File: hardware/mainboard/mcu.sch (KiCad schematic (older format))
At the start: 20 parts, among them J2 Tag-Connect SWD, J3 USB_MICRO_RIGHT, SW1 RESET, U7 ATSAMD21G18A-AUT, U8 MCP4728

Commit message: Create hardware revision mainboard v3
This addresses an issue with the ramp oscillators using the wrong type of transistor.
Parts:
- J2, TP3, TP4, TP5, TP6, TP7: dnp (none) -> 1; finalized (none) -> yes
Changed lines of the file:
@@
 Sheet 6 7
 Title "Castor & Pollux"
-Date "2020-09-26"
-Rev "v2"
+Date "2021-01-27"
+Rev "v3"
 Comp "Winterbloom"
 Comment1 "CERN-OHL-P v2"
@@
 F 2 "Connector:Tag-Connect_TC2030-IDC-NL_2x03_P1.27mm_Vertical" H 5400 7100 50  0001 C CNN
 F 3 "~" H 5400 7100 50  0001 C CNN
-F 4 "" H 5400 7100 50  0001 C CNN "finalized"
+F 4 "yes" H 5400 7100 50  0001 C CNN "finalized"
+F 5 "1" H 5400 7100 50  0001 C CNN "dnp"
 	1    5400 7100
 	1    0    0    -1
@@
 F 2 "TestPoint:TestPoint_Pad_D1.0mm" H 8050 1000 50  0001 C CNN
 F 3 "~" H 8050 1000 50  0001 C CNN
+F 4 "1" H 7850 1000 50  0001 C CNN "dnp"
+F 5 "yes" H 7850 1000 50  0001 C CNN "finalized"
 	1    7850 1000
 	0    1    1    0
@@
 F 2 "TestPoint:TestPoint_Pad_D1.0mm" H 8050 1200 50  0001 C CNN
 F 3 "~" H 8050 1200 50  0001 C CNN
+F 4 "1" H 7850 1200 50  0001 C CNN "dnp"
+F 5 "yes" H 7850 1200 50  0001 C CNN "finalized"
 	1    7850 1200
 	0    1    1    0
@@
 F 2 "TestPoint:TestPoint_Pad_D1.0mm" H 5450 7450 50  0001 C CNN
 F 3 "~" H 5450 7450 50  0001 C CNN
+F 4 "1" H 5250 7450 50  0001 C CNN "dnp"
+F 5 "yes" H 5250 7450 50  0001 C CNN "finalized"
 	1    5250 7450
 	0    1    1    0
@@
 F 2 "TestPoint:TestPoint_Pad_D1.0mm" H 5450 7650 50  0001 C CNN
 F 3 "~" H 5450 7650 50  0001 C CNN
+F 4 "1" H 5250 7650 50  0001 C CNN "dnp"
+F 5 "yes" H 5250 7650 50  0001 C CNN "finalized"
 	1    5250 7650
 	0    1    1    0
@@
 F 2 "TestPoint:TestPoint_Pad_D1.0mm" H 5450 7850 50  0001 C CNN
 F 3 "~" H 5450 7850 50  0001 C CNN
+F 4 "1" H 5250 7850 50  0001 C CNN "dnp"
+F 5 "yes" H 5250 7850 50  0001 C CNN "finalized"
 	1    5250 7850
 	0    1    1    0

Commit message: hardware: finalize v3 of mainboard for production
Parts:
- C18, C19, C20, C21, C22, C49, C50: Reqs (none) -> bypass
- C23: Reqs (none) -> audio path; mpn GRM21BR61E106KA73K -> CL21A106KAYNNNG; mpn alt (none) -> GRM21BR61E106KA73K
- R24, R25: Reqs (none) -> i2c pullup
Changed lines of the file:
@@
 Sheet 6 7
 Title "Castor & Pollux"
-Date "2021-02-01"
+Date "2021-02-05"
 Rev "v3"
 Comp "Winterbloom"
@@
 F 6 "10%, 25v" H 3050 1650 50  0001 C CNN "mpn specs"
 F 7 "GCM188R71E105KA64D" H 3050 1650 50  0001 C CNN "mpn alt"
+F 8 "bypass" H 3050 1650 50  0001 C CNN "Reqs"
 	1    3050 1650
 	1    0    0    -1
@@
 F 6 "10%, 25v" H 3150 7000 50  0001 C CNN "mpn specs"
 F 7 "GCM188R91E104KA37D" H 3150 7000 50  0001 C CNN "mpn alt"
+F 8 "bypass" H 3150 7000 50  0001 C CNN "Reqs"
 	1    3150 7000
 	1    0    0    -1
@@
 F 6 "10%, 25v" H 3650 7000 50  0001 C CNN "mpn specs"
 F 7 "GCM188R91E104KA37D" H 3650 7000 50  0001 C CNN "mpn alt"
+F 8 "bypass" H 3650 7000 50  0001 C CNN "Reqs"
 	1    3650 7000
 	1    0    0    -1
@@
 F 6 "10%, 25v" H 4150 7000 50  0001 C CNN "mpn specs"
 F 7 "GCM188R91E104KA37D" H 4150 7000 50  0001 C CNN "mpn alt"
+F 8 "bypass" H 4150 7000 50  0001 C CNN "Reqs"
 	1    4150 7000
 	1    0    0    -1
@@
 F 6 "100mW" H 4800 5900 50  0001 C CNN "mpn specs"
 F 7 "ERA-3AED472V" H 4800 5900 50  0001 C CNN "mpn alt"
+F 8 "i2c pullup" H 4800 5900 50  0001 C CNN "Reqs"
 	1    4800 5900
 	1    0    0    -1
@@
 F 6 "100mW" H 5200 5900 50  0001 C CNN "mpn specs"
 F 7 "ERA-3AED472V" H 5200 5900 50  0001 C CNN "mpn alt"
+F 8 "i2c pullup" H 5200 5900 50  0001 C CNN "Reqs"
 	1    5200 5900
 	1    0    0    -1
@@
 F 6 "10%, 25v" H 7750 5900 50  0001 C CNN "mpn specs"
 F 7 "GCM188R91E104KA37D" H 7750 5900 50  0001 C CNN "mpn alt"
+F 8 "bypass" H 7750 5900 50  0001 C CNN "Reqs"
 	1    7750 5900
 	1    0    0    -1
@@
 F 3 "~" H 8300 5900 50  0001 C CNN
 F 4 "yes" H 8300 5900 50  0001 C CNN "finalized"
-F 5 "GRM21BR61E106KA73K" H 8300 5900 50  0001 C CNN "mpn"
+F 5 "CL21A106KAYNNNG" H 8300 5900 50  0001 C CNN "mpn"
 F 6 "10% 16v" H 8300 5900 50  0001 C CNN "mpn specs"
-F 7 "" H 8300 5900 50  0001 C CNN "mpn alt"
+F 7 "GRM21BR61E106KA73K" H 8300 5900 50  0001 C CNN "mpn alt"
+F 8 "audio path" H 8300 5900 50  0001 C CNN "Reqs"
 	1    8300 5900
 	1    0    0    -1
@@
 F 6 "10%, 25v" H 2700 7000 50  0001 C CNN "mpn specs"
 F 7 "GCM188R91E104KA37D" H 2700 7000 50  0001 C CNN "mpn alt"
+F 8 "bypass" H 2700 7000 50  0001 C CNN "Reqs"
 	1    2700 7000
 	1    0    0    -1
@@
 F 6 "10%, 25v" H 2250 7000 50  0001 C CNN "mpn specs"
 F 7 "GCM188R91E104KA37D" H 2250 7000 50  0001 C CNN "mpn alt"
+F 8 "bypass" H 2250 7000 50  0001 C CNN "Reqs"
 	1    2250 7000
 	1    0    0    -1

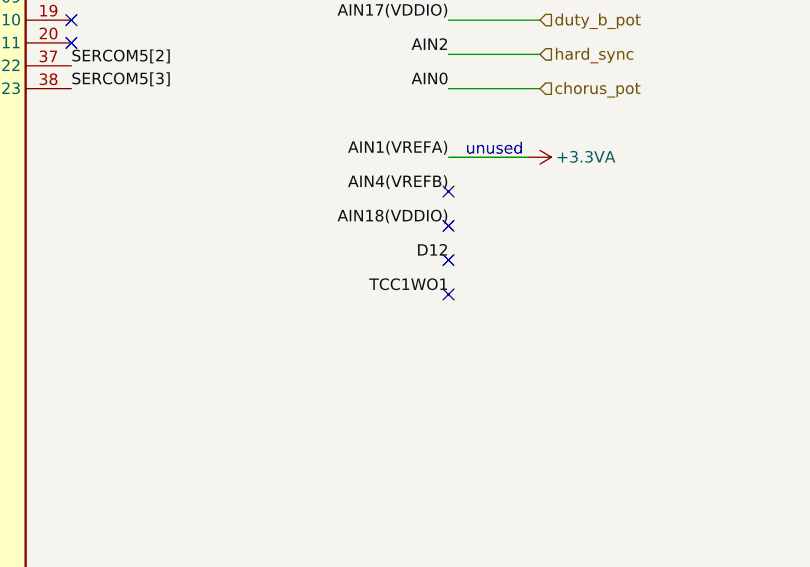
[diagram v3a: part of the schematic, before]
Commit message: hardware: finish up mpn assignments for mainboard
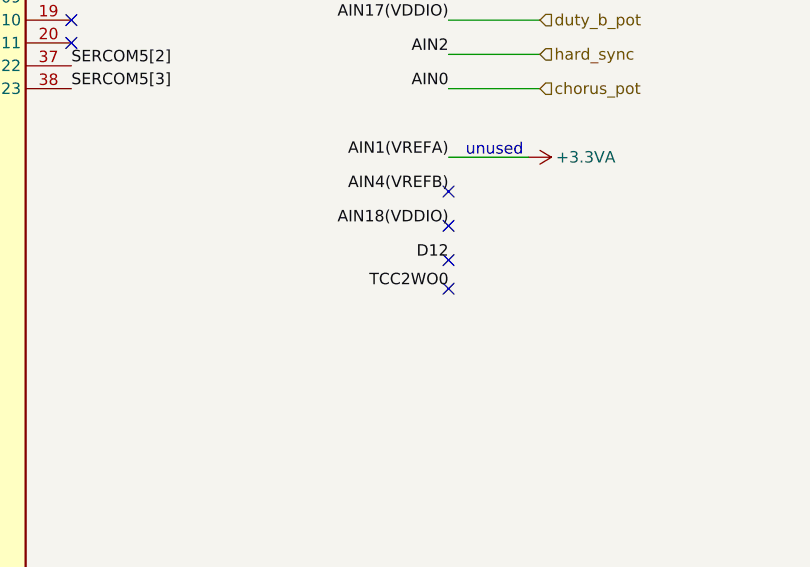
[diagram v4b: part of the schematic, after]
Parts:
- C23: Reqs audio path -> audio path, 25v; mpn CL21A106KAYNNNG -> CL21A106KAYNNN; mpn alt GRM21BR61E106KA73K -> (none); mpn specs 10% 16v -> 10% 25v
- R24, R25: mpn specs 100mW -> 100mW, 5%
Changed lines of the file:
@@
 F 4 "yes" H 4800 5900 50  0001 C CNN "finalized"
 F 5 "MF-RES-0603-4.7K" H 4800 5900 50  0001 C CNN "mpn"
-F 6 "100mW" H 4800 5900 50  0001 C CNN "mpn specs"
+F 6 "100mW, 5%" H 4800 5900 50  0001 C CNN "mpn specs"
 F 7 "ERA-3AED472V" H 4800 5900 50  0001 C CNN "mpn alt"
 F 8 "i2c pullup" H 4800 5900 50  0001 C CNN "Reqs"
@@
 F 4 "yes" H 5200 5900 50  0001 C CNN "finalized"
 F 5 "MF-RES-0603-4.7K" H 5200 5900 50  0001 C CNN "mpn"
-F 6 "100mW" H 5200 5900 50  0001 C CNN "mpn specs"
+F 6 "100mW, 5%" H 5200 5900 50  0001 C CNN "mpn specs"
 F 7 "ERA-3AED472V" H 5200 5900 50  0001 C CNN "mpn alt"
 F 8 "i2c pullup" H 5200 5900 50  0001 C CNN "Reqs"
@@
 F 3 "~" H 8300 5900 50  0001 C CNN
 F 4 "yes" H 8300 5900 50  0001 C CNN "finalized"
-F 5 "CL21A106KAYNNNG" H 8300 5900 50  0001 C CNN "mpn"
-F 6 "10% 16v" H 8300 5900 50  0001 C CNN "mpn specs"
-F 7 "GRM21BR61E106KA73K" H 8300 5900 50  0001 C CNN "mpn alt"
-F 8 "audio path" H 8300 5900 50  0001 C CNN "Reqs"
+F 5 "CL21A106KAYNNN" H 8300 5900 50  0001 C CNN "mpn"
+F 6 "10% 25v" H 8300 5900 50  0001 C CNN "mpn specs"
+F 7 "" H 8300 5900 50  0001 C CNN "mpn alt"
+F 8 "audio path, 25v" H 8300 5900 50  0001 C CNN "Reqs"
 	1    8300 5900
 	1    0    0    -1
@@
 AIN18(VDDIO)
 NoConn ~ 5500 3550
-Text Label 5500 3850 2    50   ~ 0
-TCC1WO1
-NoConn ~ 5500 3850
 Text Notes 6900 6400 0    50   ~ 0
 0.8mA (typ)\n1.4mA (max)
@@
 Text Notes 5575 3250 0    50   ~ 0
 unused
+Text Label 5500 3825 2    50   ~ 0
+TCC2WO0
+NoConn ~ 5500 3825
 $EndSCHEMATC
